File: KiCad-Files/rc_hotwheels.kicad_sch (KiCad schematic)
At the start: 6 parts, among them IC1 BD6211F-E2, M1 Motor_DC, U1 STM32F070F6P6, U3 NRF24L01_Breakout

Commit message: Motor connections and configurations updated(Forward, Reverse, Speed)
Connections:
- net PA9: now also IC1.6 (VREF)
- net VREF: now reaches U1.17 (PA9)
- net FIN: now reaches U1.6 (PA0)
- net RIN: now reaches U1.7 (PA1)
- net PA0: now reaches IC1.4 (FIN)
- net PA1: now reaches IC1.5 (RIN)
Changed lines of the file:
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@@
+    (stroke (width 0) (type default))
+  )
+  (wire (pts (xy 201.93 41.91) (xy 207.01 41.91))
     (stroke (width 0) (type default))
   )
@@
   )
   (wire (pts (xy 31.75 182.88) (xy 40.64 182.88))
+    (stroke (width 0) (type default))
+  )
+  (wire (pts (xy 205.74 59.69) (xy 207.01 59.69))
     (stroke (width 0) (type default))
   )
@@
     (effects (font (size 1.27 1.27)) (justify left top))
   )
+  (global_label "PA1" (shape input) (at 72.39 186.69 0) (fields_autoplaced)
+    (effects (font (size 1.27 1.27)) (justify left))
+    (property "Intersheetrefs" "${INTERSHEET_REFS}" (at 78.9433 186.69 0)
+      (effects (font (size 1.27 1.27)) (justify left) hide)
+    )
+    (property "Motor Forward" "" (at 72.39 188.8808 0)
+      (effects (font (size 1.27 1.27)) (justify left))
+    )
+  )
   (global_label "PA9" (shape input) (at 33.02 68.58 180) (fields_autoplaced)
     (effects (font (size 1.27 1.27)) (justify right))
@@
     )
   )
+  (global_label "PA9" (shape input) (at 72.39 184.15 0) (fields_autoplaced)
+    (effects (font (size 1.27 1.27)) (justify left))
+    (property "Intersheetrefs" "${INTERSHEET_REFS}" (at 78.9433 184.15 0)
+      (effects (font (size 1.27 1.27)) (justify left) hide)
+    )
+    (property "Motor Speed" "" (at 72.39 186.3408 0)
+      (effects (font (size 1.27 1.27)) (justify left))
+    )
+  )
+  (global_label "RIN" (shape input) (at 201.93 41.91 180) (fields_autoplaced)
+    (effects (font (size 1.27 1.27)) (justify right))
+    (property "Intersheetrefs" "${INTERSHEET_REFS}" (at 195.7395 41.91 0)
+      (effects (font (size 1.27 1.27)) (justify right) hide)
+    )
+    (property "Motor Reverse" "" (at 201.93 44.1008 0)
+      (effects (font (size 1.27 1.27)) (justify right))
+    )
+  )
   (global_label "PA6" (shape input) (at 38.1 106.68 180) (fields_autoplaced)
     (effects (font (size 1.27 1.27)) (justify right))
@@
     )
   )
+  (global_label "FIN" (shape input) (at 207.01 39.37 180) (fields_autoplaced)
+    (effects (font (size 1.27 1.27)) (justify right))
+    (property "Intersheetrefs" "${INTERSHEET_REFS}" (at 201.0009 39.37 0)
+      (effects (font (size 1.27 1.27)) (justify right) hide)
+    )
+    (property "Motor Forward" "" (at 207.01 41.5608 0)
+      (effects (font (size 1.27 1.27)) (justify right))
+    )
+  )
+  (global_label "VREF" (shape input) (at 205.74 59.69 180) (fields_autoplaced)
+    (effects (font (size 1.27 1.27)) (justify right))
+    (property "Intersheetrefs" "${INTERSHEET_REFS}" (at 198.1586 59.69 0)
+      (effects (font (size 1.27 1.27)) (justify right) hide)
+    )
+    (property "Motor Speed" "" (at 205.74 61.8808 0)
+      (effects (font (size 1.27 1.27)) (justify right))
+    )
+  )
   (global_label "PA5" (shape input) (at 38.1 110.49 180) (fields_autoplaced)
     (effects (font (size 1.27 1.27)) (justify right))
@@
     )
   )
+  (global_label "PA0" (shape input) (at 41.91 186.69 180) (fields_autoplaced)
+    (effects (font (size 1.27 1.27)) (justify right))
+    (property "Intersheetrefs" "${INTERSHEET_REFS}" (at 35.3567 186.69 0)
+      (effects (font (size 1.27 1.27)) (justify right) hide)
+    )
+    (property "Motor Forward" "" (at 41.91 188.8808 0)
+      (effects (font (size 1.27 1.27)) (justify right))
+    )
+  )

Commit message: Servo motor connection and configurations updated.
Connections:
- net PA9: no longer S_M1.1 (PWM)
- net PWM: now reaches U1.10 (PA4)
- new net PA4: S_M1.1 (PWM)
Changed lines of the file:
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@@
     )
   )
-  (global_label "PA9" (shape input) (at 33.02 68.58 180) (fields_autoplaced)
+  (global_label "PA4" (shape input) (at 33.02 68.58 180) (fields_autoplaced)
     (effects (font (size 1.27 1.27)) (justify right))
-    (property "Intersheetrefs" "${INTERSHEET_REFS}" (at 26.5461 68.58 0)
+    (property "Intersheetrefs" "${INTERSHEET_REFS}" (at 26.4667 68.58 0)
+      (effects (font (size 1.27 1.27)) (justify right) hide)
+    )
+    (property "Servo Control" "" (at 33.02 70.7708 0)
       (effects (font (size 1.27 1.27)) (justify right) hide)
     )
@@
       (effects (font (size 1.27 1.27)) (justify right))
     )
+  )
+  (global_label "PWM" (shape input) (at 207.01 49.53 180) (fields_autoplaced)
+    (effects (font (size 1.27 1.27)) (justify right))
+    (property "Intersheetrefs" "${INTERSHEET_REFS}" (at 199.852 49.53 0)
+      (effects (font (size 1.27 1.27)) (justify right) hide)
+    )
+    (property "SERVO Control" "" (at 207.01 51.7208 0)
+      (effects (font (size 1.27 1.27)) (justify right))
+    )

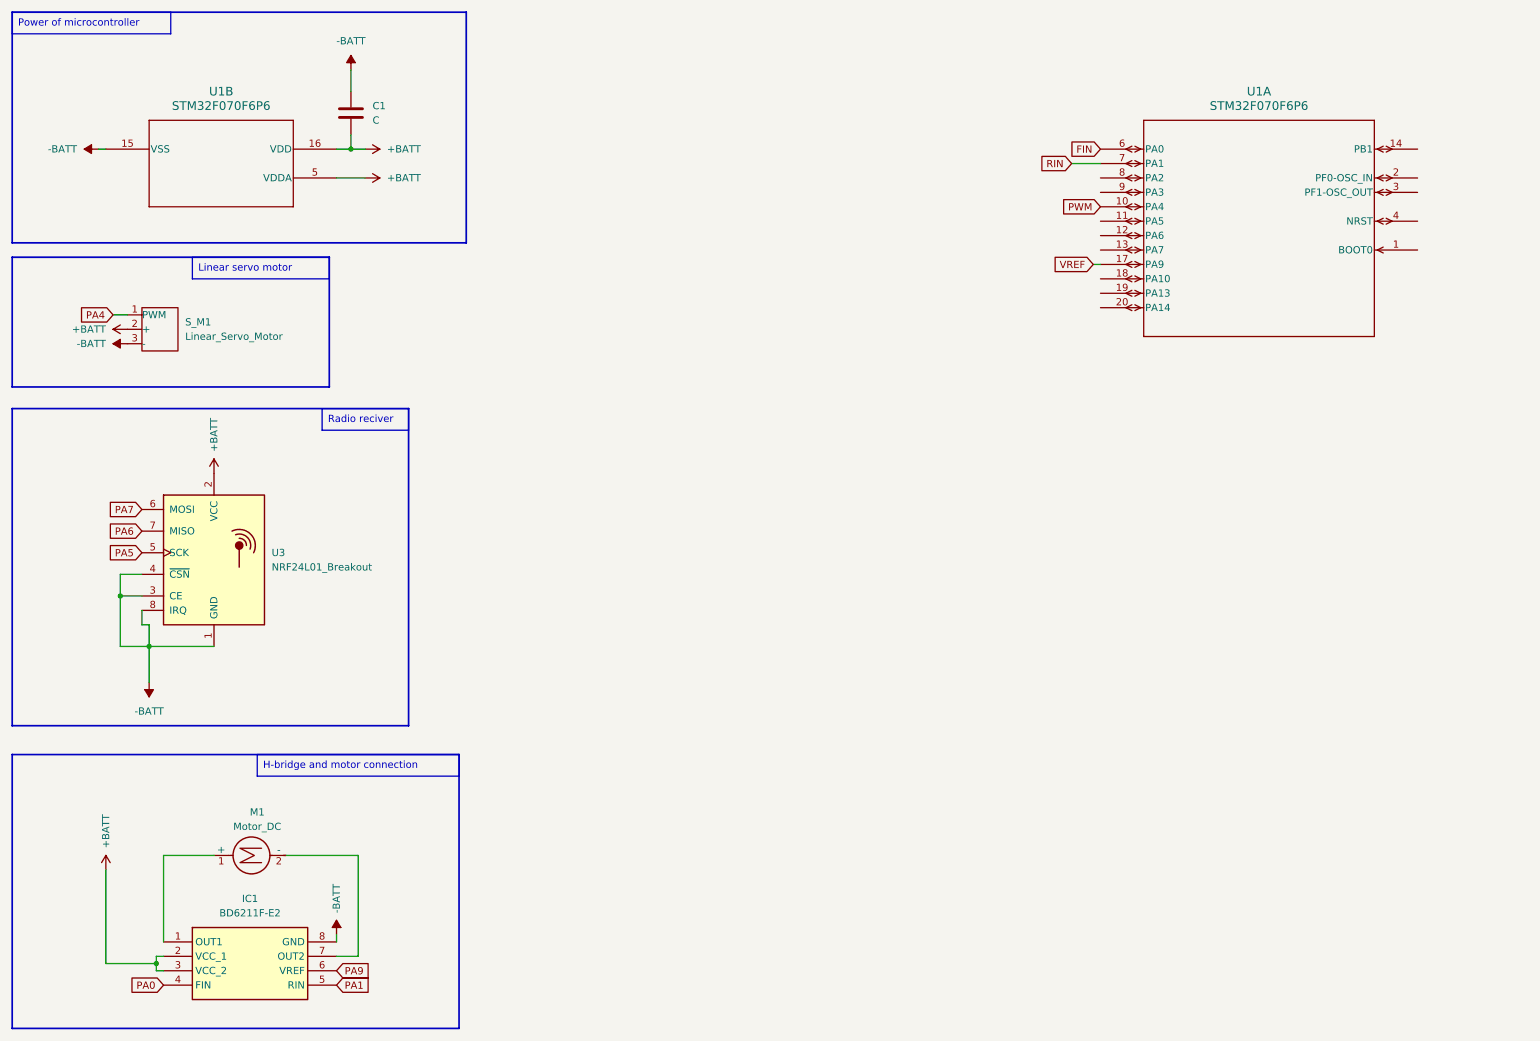
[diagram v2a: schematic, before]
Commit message: Added Voltage Regulator symbol, connections and improved STM pinout user label
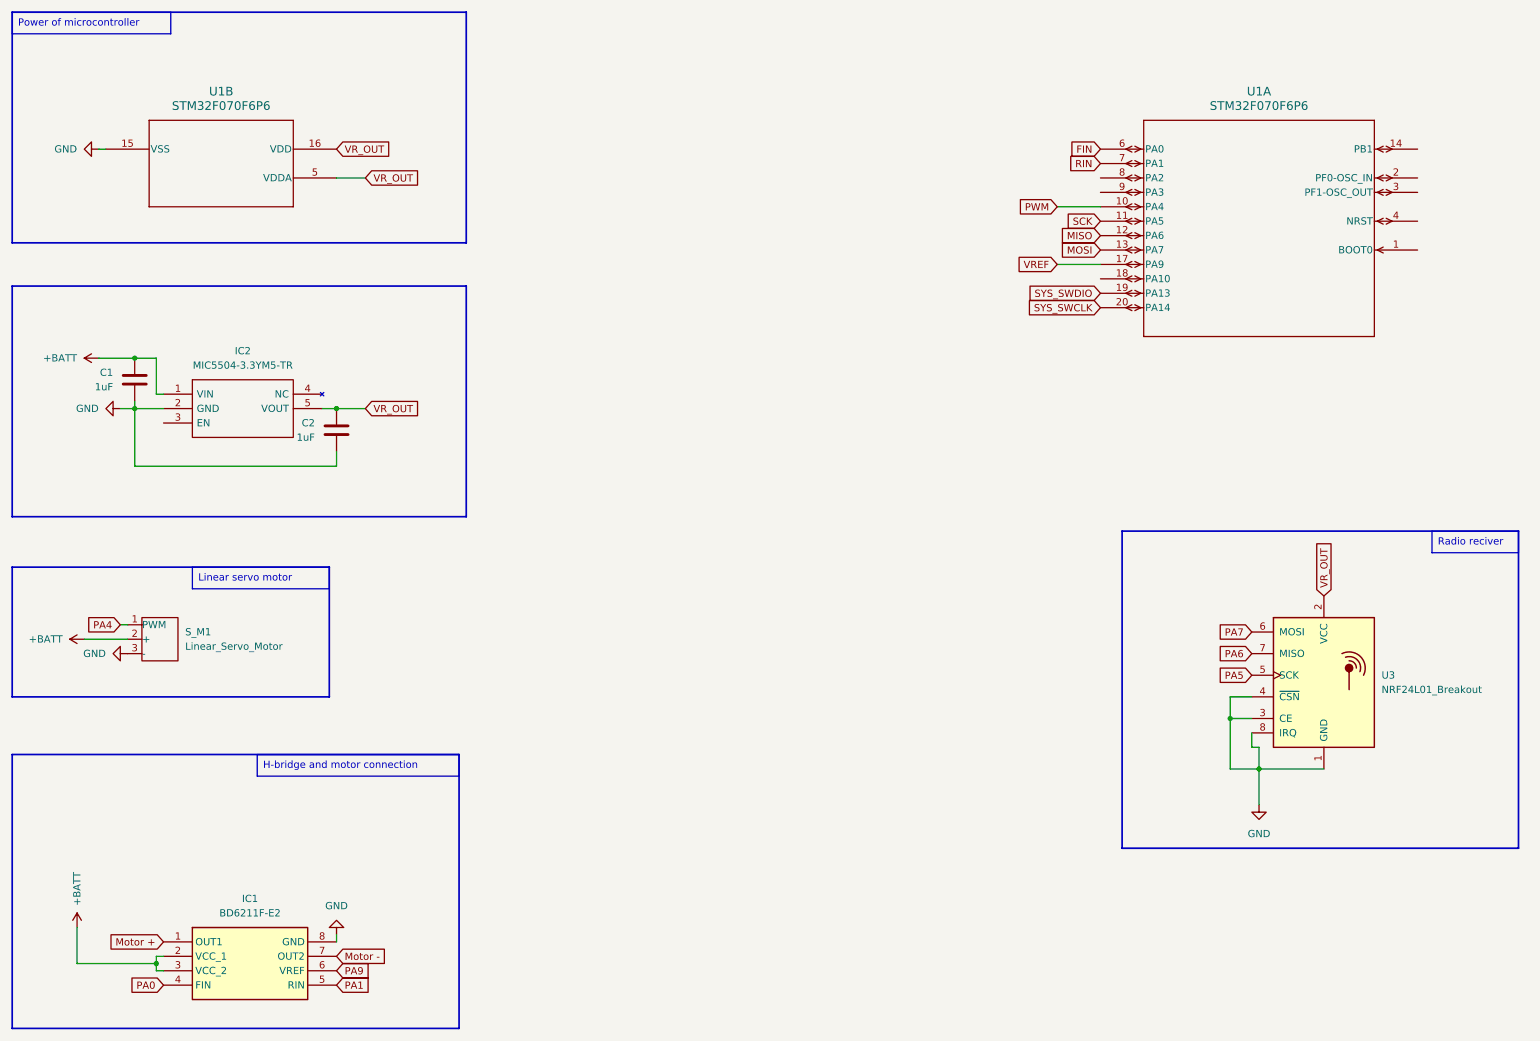
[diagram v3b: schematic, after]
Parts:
- removed M1: Motor_DC, symbol Motor:Motor_DC
- added C2: 1uF, symbol Device:C
- added IC2: MIC5504-3.3YM5-TR, SOT95P280X145-5N, symbol MIC5504-3.3YM5-TR:MIC5504-3.3YM5-TR
- C1: value C -> 1uF
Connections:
- net +BATT: now also C1.2, IC2.1 (VIN); no longer C1.1, U1.16 (VDD), U1.5 (VDDA), U3.2 (VCC)
- net SCK: now reaches U1.11 (PA5)
- net MISO: now reaches U1.12 (PA6)
- net MOSI: now reaches U1.13 (PA7)
- net SYS_SWDIO: now reaches U1.19 (PA13)
- net SYS_SWCLK: now reaches U1.20 (PA14)
- net Motor +: now reaches IC1.1 (OUT1)
- net Motor -: now reaches IC1.7 (OUT2)
- net -BATT renamed GND
- net GND: now also C1.1, C2.1, IC2.2 (GND); no longer C1.2
- new net VR_OUT: C2.2, IC2.5 (VOUT), U1.16 (VDD), U1.5 (VDDA), U3.2 (VCC)
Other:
- moved on the sheet: S_M1, U3

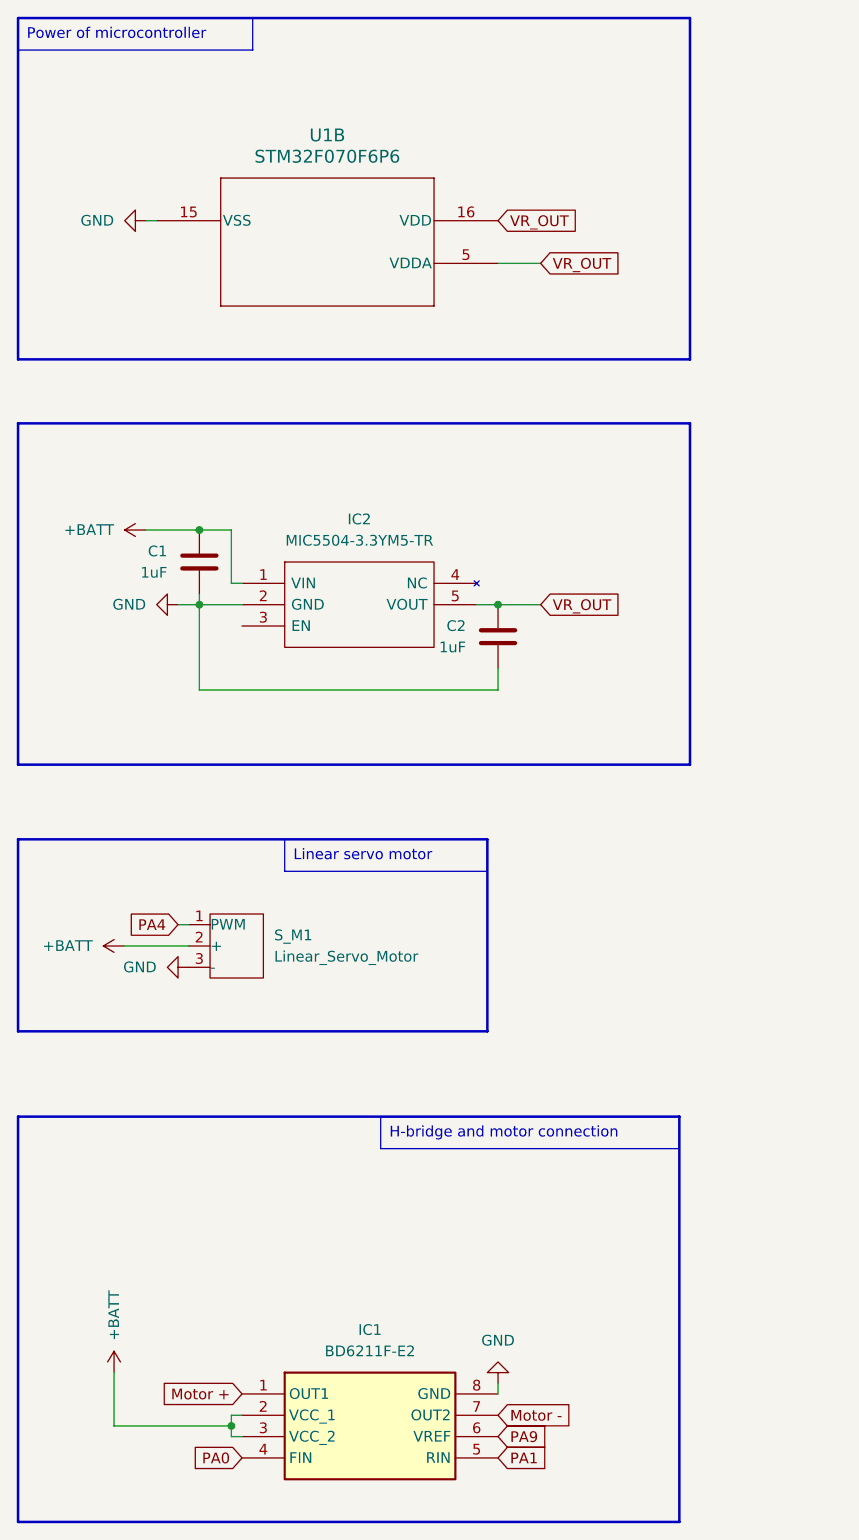
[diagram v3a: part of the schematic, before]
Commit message: Added capacitors to the MCU and Voltage Regulator
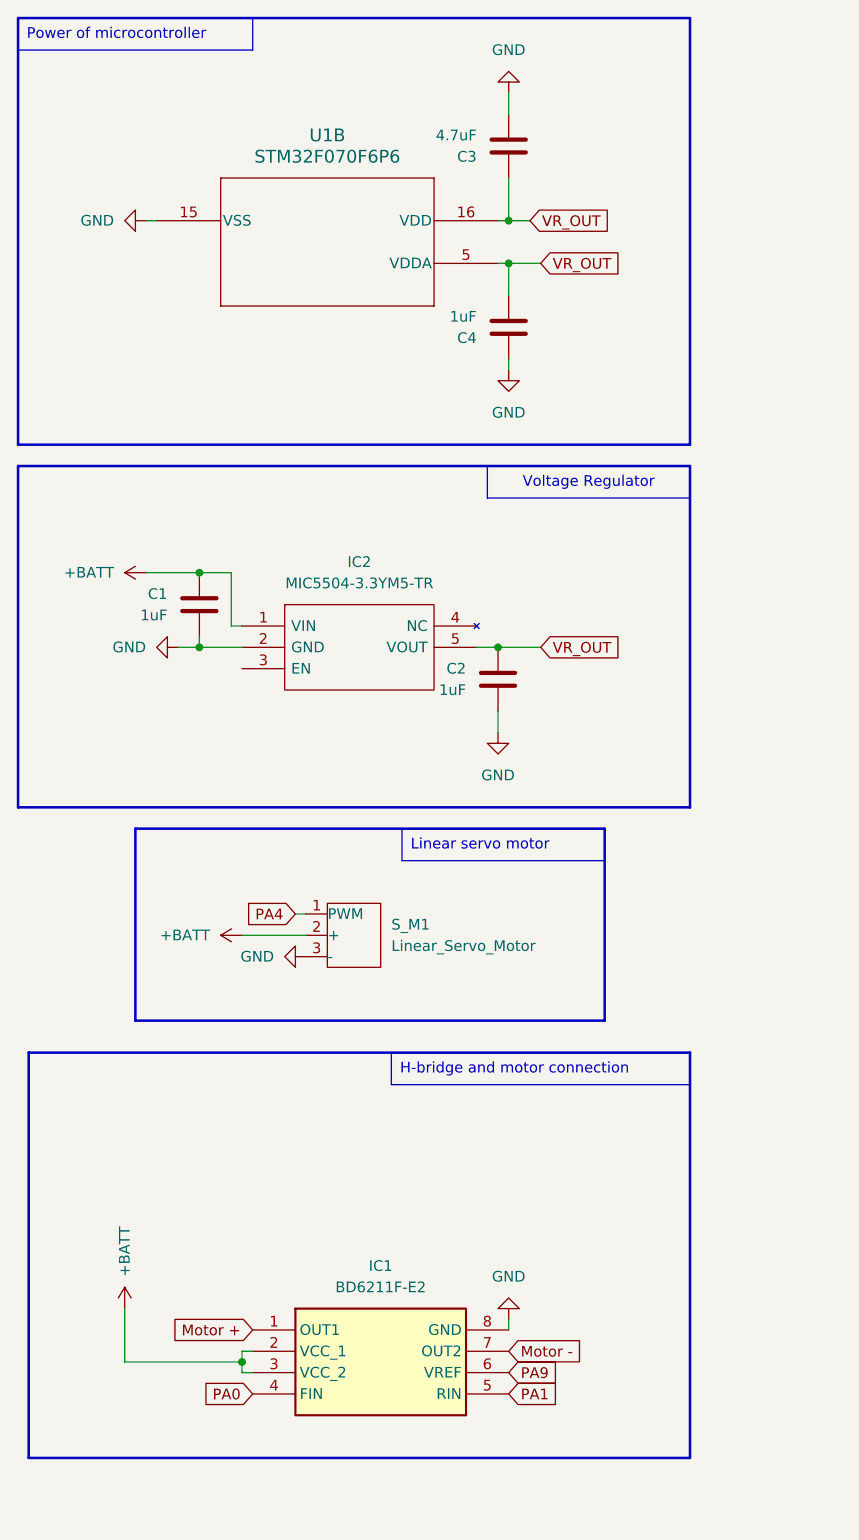
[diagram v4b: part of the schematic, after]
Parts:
- added C3: 4.7uF, symbol Device:C
- added C4: 1uF, symbol Device:C
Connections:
- net GND: now also C3.1, C4.2
- net VR_OUT: now also C3.2, C4.1
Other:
- moved on the sheet: C1, C2, IC1, IC2, S_M1

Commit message: Capacitors footprints added
Capacitor_THT:C_Rect_L4.6mm_W2.0mm_P2.50mm_MKS02_FKP02
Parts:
- C1, C2, C3, C4: footprint (none) -> Capacitor_THT:C_Rect_L4.6mm_W2.0mm_P2.50mm_MKS02_FKP02
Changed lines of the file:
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@@
       (effects (font (size 1.27 1.27)) (justify right))
     )
-    (property "Footprint" "" (at 37.7952 81.28 0)
+    (property "Footprint" "Capacitor_THT:C_Rect_L4.6mm_W2.0mm_P2.50mm_MKS02_FKP02" (at 37.7952 81.28 0)
       (effects (font (size 1.27 1.27)) hide)
     )
@@
       (effects (font (size 1.27 1.27)) (justify right))
     )
-    (property "Footprint" "" (at 74.6252 34.29 0)
+    (property "Footprint" "Capacitor_THT:C_Rect_L4.6mm_W2.0mm_P2.50mm_MKS02_FKP02" (at 74.6252 34.29 0)
       (effects (font (size 1.27 1.27)) hide)
     )
@@
       (effects (font (size 1.27 1.27)) (justify right))
     )
-    (property "Footprint" "" (at 74.6252 55.88 0)
+    (property "Footprint" "Capacitor_THT:C_Rect_L4.6mm_W2.0mm_P2.50mm_MKS02_FKP02" (at 74.6252 55.88 0)
       (effects (font (size 1.27 1.27)) hide)
     )
@@
       (effects (font (size 1.27 1.27)) (justify right))
     )
-    (property "Footprint" "" (at 73.3552 90.17 0)
-      (effects (font (size 1.27 1.27)) hide)
-    )
+    (property "Footprint" "Capacitor_THT:C_Rect_L4.6mm_W2.0mm_P2.50mm_MKS02_FKP02" (at 73.3552 90.17 0)
+      (effects (font (size 1.27 1.27)) hide)
+    )
